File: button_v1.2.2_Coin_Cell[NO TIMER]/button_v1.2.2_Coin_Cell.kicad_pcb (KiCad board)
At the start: 2 copper layers, 21 x 47.8 mm, 18 parts, among them J1 Conn_01x05_Female, SW1 SW_Push, SW2 SW_Push, U1 TPS61097A, X1 ESP-12E

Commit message: 23.02 00:38
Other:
- board text added: "LK"

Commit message: :rocket: :full_moon_with_face:
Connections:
- D1 pad 1: /GND -> /VCC
- R6 pad 2: Net-(R6-Pad2) -> /RST
- SW1 pad 2: Net-(R6-Pad2) -> /GND
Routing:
- net /GND: track 70.3 -> 82.5 mm, vias 12 -> 14
- net Net-(R6-Pad2): track 9.20 -> 0.00 mm
- net /VCC: track 49.7 -> 57.4 mm
- net /RST: track 57.8 -> 59.1 mm, vias 2 -> 3
- net Net-(R7-Pad2): track 4.14 -> 3.35 mm

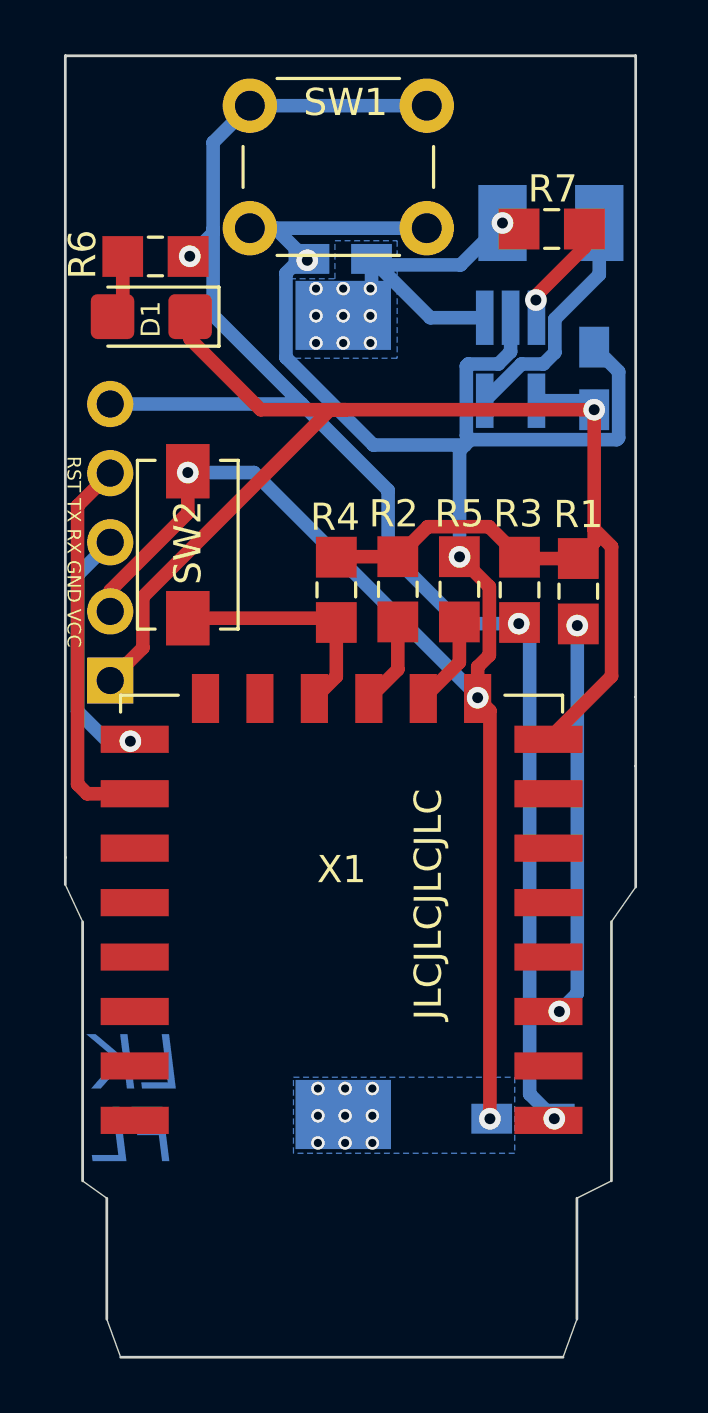
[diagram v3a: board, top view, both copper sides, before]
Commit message: 3D Models etwas verbessert
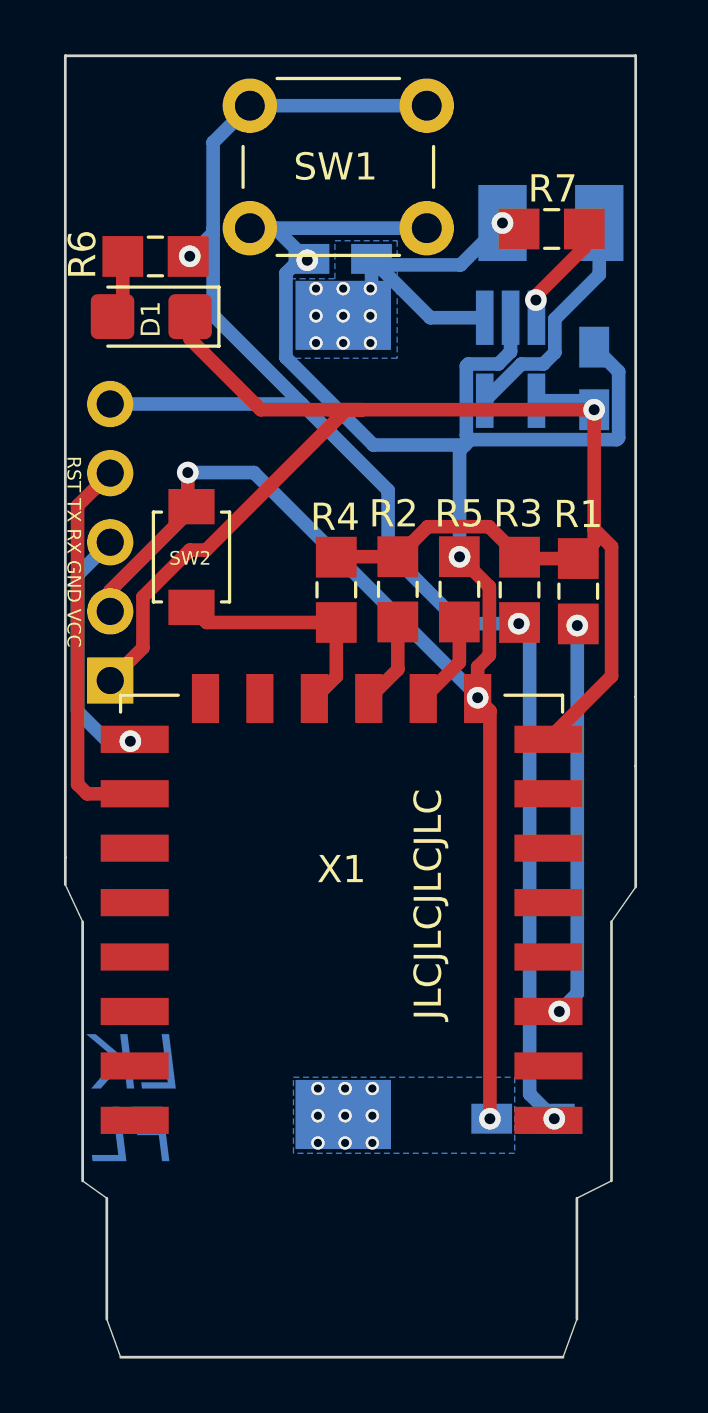
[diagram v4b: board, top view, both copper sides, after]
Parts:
- J1: footprint Connector_PinHeader_2.54mm:PinHeader_1x05_P2.54mm_Vertical -> handsolder:PinSocket_1x05_P2.54mm_Vertical_mod
- SW1: footprint Button_Switch_THT:SW_PUSH_6mm -> handsolder:SW_PUSH_6mm_H8mm_mod
- SW2: footprint Button_Switch_SMD:SW_SPST_EVQPE1 -> handsolder:SW_SPST_B3U-1000P_mod
- moved SW2 0.47 mm to (120.2, 73.0)
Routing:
- net /VCC: track 57.4 -> 58.5 mm

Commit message: cap between esp vcc and ground added
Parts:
- added C4: TAJB476M010TNJ, SamacSys_Parts:CAPPM3528X210N, F.Cu at (133.5, 70.2)
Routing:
- net /GND: track 82.5 -> 84.8 mm, vias 14 -> 15
- net /VCC: track 58.5 -> 59.9 mm

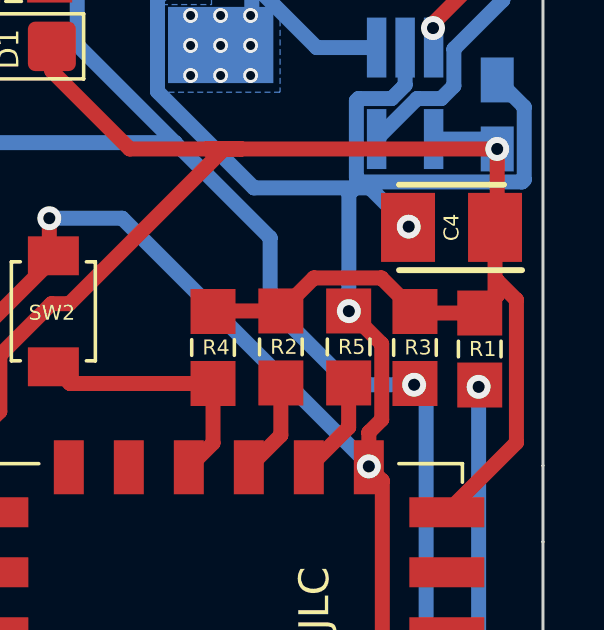
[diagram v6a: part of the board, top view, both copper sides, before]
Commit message: Added 100nF decoupling capacitors between VCC and Ground of the ESP
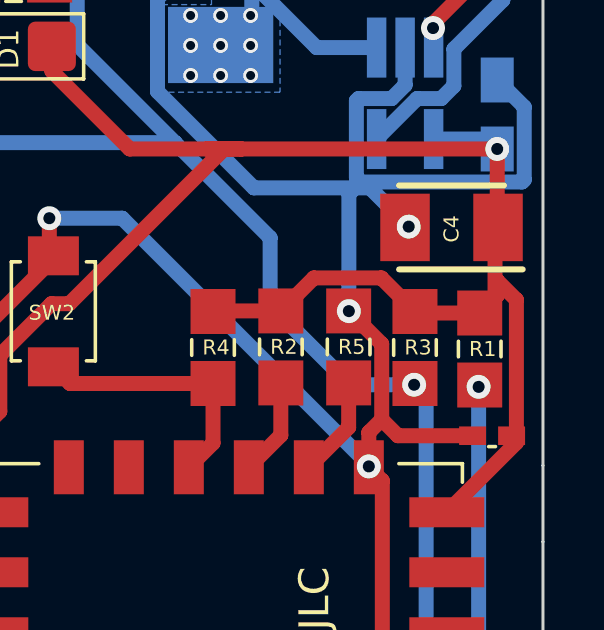
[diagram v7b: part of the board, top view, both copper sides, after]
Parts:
- added C5: 100nF, handsolder:C_0402_1005Metric_Pad0.74x0.62mm_HandSoldermod, F.Cu at (134.8, 77.1)
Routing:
- net /GND: track 84.8 -> 88.1 mm
